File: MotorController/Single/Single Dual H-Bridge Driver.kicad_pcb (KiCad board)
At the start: 2 copper layers, 15 parts, among them J1 RJ45, K1 CONN_3, M1 MOTOR, P1 H Power input, Q1 C_MOSF, Q2 C_MOSF, Q3 C_MOSF, Q4 C_MOSF

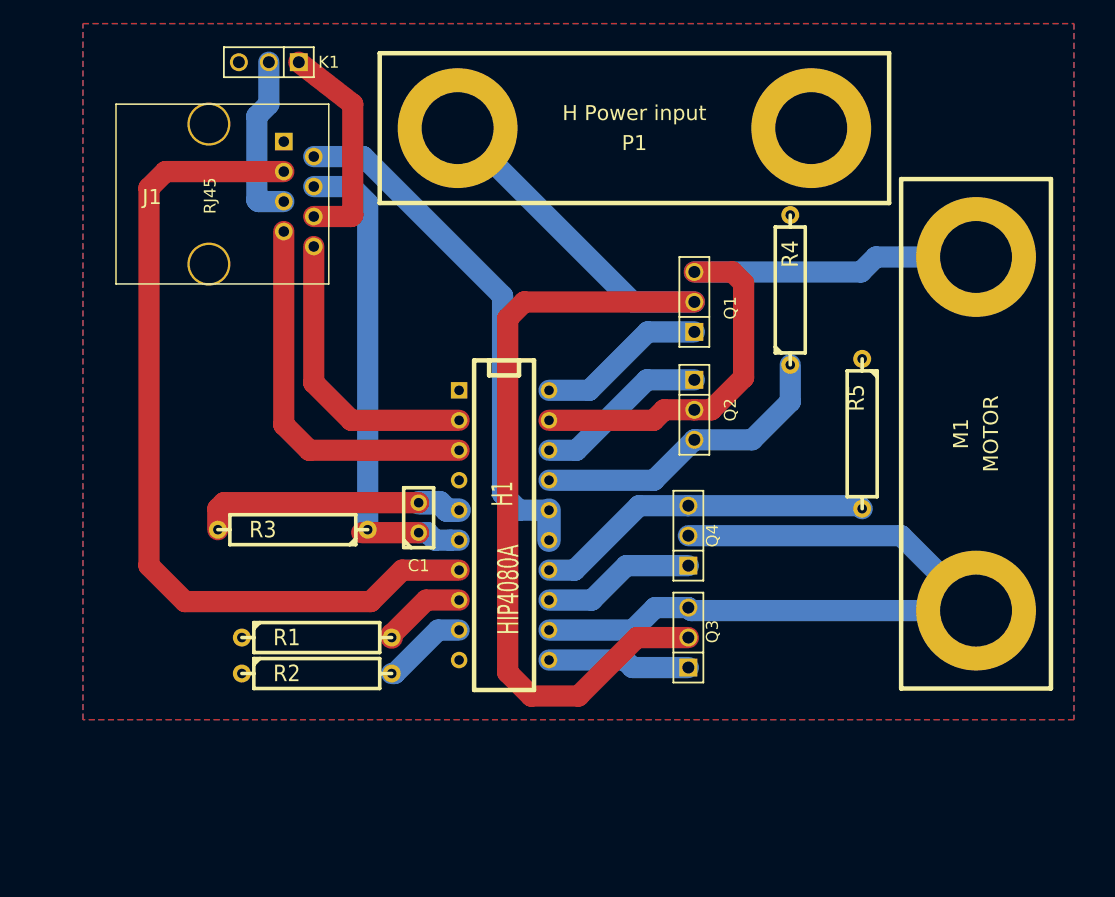
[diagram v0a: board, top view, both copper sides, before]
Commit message: updating various changes in codebase , adding in new esp32 directory for code running on the esp32
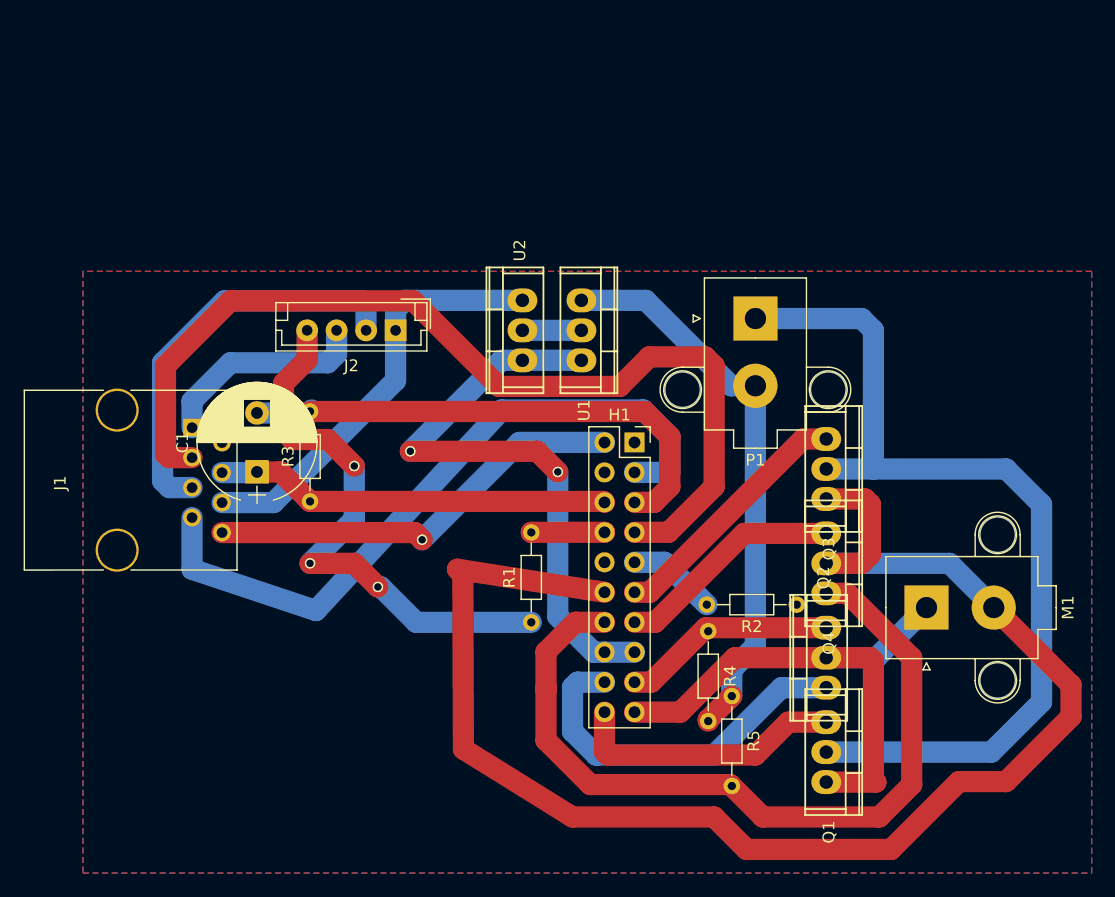
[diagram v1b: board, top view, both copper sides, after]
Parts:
- removed K1: CONN_3, PIN_ARRAY_3X1
- added J2: CONN_01X04, Connectors_JST:JST_EH_B04B-EH-A_04x2.50mm_Straight, F.Cu at (90.5, 40.0)
- added U1: LM7812, cpyarger:CPTO-220, F.Cu at (106.2, 40.0)
- added U2: LM7805, cpyarger:CPTO-220, F.Cu at (101.2, 40.0)
- C1: footprint C1 -> Capacitors_THT:CP_Radial_D10.0mm_P5.00mm
- H1: footprint DIP-20__300 -> Socket_Strips:Socket_Strip_Straight_2x10_Pitch2.54mm
- J1: footprint RJ45_8 -> Connectors:RJ45_8
- M1: footprint 2PIN_6mm -> Connectors_Molex:Molex_MegaFit_2x01x5.70mm_Straight
- P1: value H Power input -> CONN_2; footprint 2PIN_6mm -> Connectors_Molex:Molex_MegaFit_2x01x5.70mm_Straight
- Q1, Q2, Q3, Q4: footprint PIN_ARRAY_3X1 -> cp:CPTO-220
- R1, R2, R3, R4, R5: footprint R5 -> Resistors_THT:R_Axial_DIN0204_L3.6mm_D1.6mm_P7.62mm_Horizontal
- moved R2 41.1 mm to (124.5, 63.2), turned to 180 degrees
- moved Q1 39.8 mm to (127.0, 75.8), turned to 270 degrees
- moved R4 29.7 mm to (117.0, 65.5), turned to 270 degrees
- moved R5 24.8 mm to (119.0, 71.0)
- moved Q2 23.8 mm to (127.0, 67.8), turned to 90 degrees
- moved J1 19.9 mm to (73.2, 48.2)
- moved P1 19.1 mm to (121.0, 39.0)
- moved Q3 18.5 mm to (127.0, 51.8), turned to 270 degrees
- moved R1 18.2 mm to (102.0, 64.8), turned to 90 degrees
- moved M1 15.3 mm to (135.5, 63.5), turned to 90 degrees
- moved C1 14.2 mm to (78.8, 52.0)
- moved H1 13.1 mm to (110.8, 49.5), turned to 0 degrees
- moved Q4 11.9 mm to (127.0, 59.8), turned to 270 degrees
- moved R3 2.81 mm to (83.2, 54.5), turned to 90 degrees
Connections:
- H1 pad 15: N-000005 -> Net-(H1-Pad15)
- H1 pad 16: N-000005 -> Net-(H1-Pad15)
- H1 pad 4: N-0000020 -> GND
- J1 pad 1: N-0000020 -> Net-(J1-Pad1)
- J1 pad 2: N-000005 -> (no net)
- R1 pad 1: N-0000020 -> GND
- R2 pad 1: N-0000020 -> GND
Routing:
- net Net-(H1-Pad12): track 64.5 -> 127.0 mm
- net Net-(H1-Pad15): track 0.00 -> 50.9 mm, vias 0 -> 2
- net Net-(P1-Pad2): track 0.00 -> 47.8 mm
- net GND: track 0.00 -> 47.2 mm, vias 0 -> 3
- net N-000005: track 44.7 -> 0.00 mm
- net Net-(H1-Pad14): track 28.9 -> 68.8 mm
- net Net-(H1-Pad3): track 32.1 -> 59.8 mm
- net Net-(C1-Pad2): track 22.7 -> 43.9 mm
- net Net-(J1-Pad5): track 14.4 -> 34.5 mm
- net Net-(J1-Pad1): track 0.00 -> 18.2 mm
- net Net-(J1-Pad6): track 18.5 -> 36.1 mm
- net Net-(H1-Pad18): track 14.8 -> 31.3 mm
- net Net-(P1-Pad1): track 91.0 -> 78.4 mm
- net Net-(H1-Pad2): track 25.2 -> 36.1 mm, vias 0 -> 1
- net Net-(H1-Pad11): track 12.3 -> 21.6 mm
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- added copper zone on B.Cu, net GND
- added copper zone on F.Cu, net GND
- removed copper zone on B.Cu, net N-0000020
- removed copper zone on F.Cu, net Net-(P1-Pad2)
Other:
- net class signal added: clearance 0.254, trace_width 1, via_dia 0.889, via_drill 0.635
